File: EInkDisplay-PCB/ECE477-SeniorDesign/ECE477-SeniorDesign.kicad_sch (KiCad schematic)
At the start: 1 part

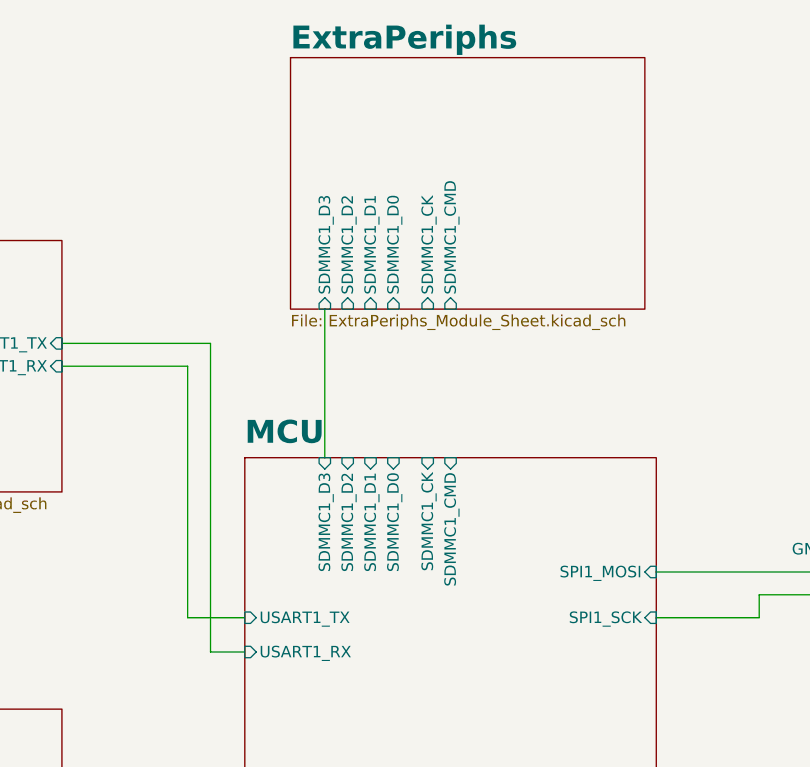
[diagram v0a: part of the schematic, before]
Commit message: Fixing SD w SPI
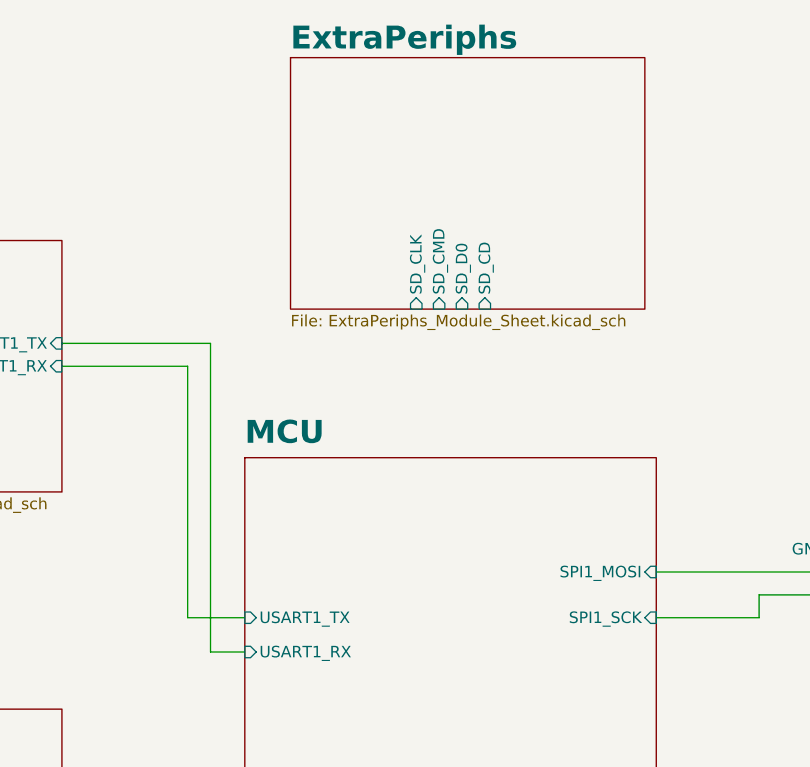
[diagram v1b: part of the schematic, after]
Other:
- sheet ExtraPeriphs ports: added SD_CD, SD_CLK, SD_CMD, SD_D0; removed SDMMC1_CK, SDMMC1_CMD, SDMMC1_D0, SDMMC1_D1, SDMMC1_D2, SDMMC1_D3
- sheet MCU ports: added none; removed SDMMC1_CK, SDMMC1_CMD, SDMMC1_D0, SDMMC1_D1, SDMMC1_D2, SDMMC1_D3
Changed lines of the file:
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@@
-	(wire
-		(pts
-			(xy 125.73 69.85) (xy 125.73 86.36)
-		)
-		(stroke
-			(width 0)
-			(type default)
-		)
-	)
 	(wire
 		(pts
@@
 			)
 		)
-		(pin "SDMMC1_D2" input
-			(at 128.27 69.85 270)
-			(effects
-				(font
-					(size 1.27 1.27)
-				)
-				(justify left)
-			)
-		)
-		(pin "SDMMC1_D3" input
-			(at 125.73 69.85 270)
-			(effects
-				(font
-					(size 1.27 1.27)
-				)
-				(justify left)
-			)
-		)
-		(pin "SDMMC1_D1" input
-			(at 130.81 69.85 270)
-			(effects
-				(font
-					(size 1.27 1.27)
-				)
-				(justify left)
-			)
-		)
-		(pin "SDMMC1_D0" input
-			(at 133.35 69.85 270)
-			(effects
-				(font
-					(size 1.27 1.27)
-				)
-				(justify left)
-			)
-		)
-		(pin "SDMMC1_CK" input
-			(at 137.16 69.85 270)
-			(effects
-				(font
-					(size 1.27 1.27)
-				)
-				(justify left)
-			)
-		)
-		(pin "SDMMC1_CMD" input
-			(at 139.7 69.85 270)
+		(pin "SD_CLK" input
+			(at 135.89 69.85 270)
+			(effects
+				(font
+					(size 1.27 1.27)
+				)
+				(justify left)
+			)
+		)
+		(pin "SD_CMD" input
+			(at 138.43 69.85 270)
+			(effects
+				(font
+					(size 1.27 1.27)
+				)
+				(justify left)
+			)
+		)
+		(pin "SD_D0" input
+			(at 140.97 69.85 270)
+			(effects
+				(font
+					(size 1.27 1.27)
+				)
+				(justify left)
+			)
+		)
+		(pin "SD_CD" input
+			(at 143.51 69.85 270)
 			(effects
 				(font
@@
 			(effects
 				(font
-					(size 1.27 1.27)
-				)
-				(justify right)
-			)
-		)
-		(pin "SDMMC1_CK" input
-			(at 137.16 86.36 90)
-			(effects
-				(font
-					(size 1.27 1.27)
-				)
-				(justify right)
-			)
-		)
-		(pin "SDMMC1_CMD" input
-			(at 139.7 86.36 90)
-			(effects
-				(font
-					(size 1.27 1.27)
-				)
-				(justify right)
-			)
-		)
-		(pin "SDMMC1_D0" input
-			(at 133.35 86.36 90)
-			(effects
-				(font
-					(size 1.27 1.27)
-				)
-				(justify right)
-			)
-		)
-		(pin "SDMMC1_D1" input
-			(at 130.81 86.36 90)
-			(effects
-				(font
-					(size 1.27 1.27)
-				)
-				(justify right)
-			)
-		)
-		(pin "SDMMC1_D2" input
-			(at 128.27 86.36 90)
-			(effects
-				(font
-					(size 1.27 1.27)
-				)
-				(justify right)
-			)
-		)
-		(pin "SDMMC1_D3" input
-			(at 125.73 86.36 90)
-			(effects
-				(font

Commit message: push
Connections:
- net MCU/SPI1_MOSI: no longer EinkDispCon2.3 (DIN)
- net MCU/SPI1_SCK: no longer EinkDispCon2.4 (CLK)
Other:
- sheet ExtraPeriphs ports: added SD_CS, SD_MISO, SD_MOSI, button1, button2, button3; removed SD_CMD, SD_D0
- sheet MCU ports: added SD_GPIO, SPI2_MISO, SPI2_MOSI, SPI2_NSS, SPI2_SCK; removed none
- moved on the sheet: EinkDispCon2
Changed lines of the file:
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@@
+	(wire
+		(pts
+			(xy 133.35 69.85) (xy 133.35 86.36)
+		)
+		(stroke
+			(width 0)
+			(type default)
+		)
+	)
 	(wire
 		(pts
@@
 	(wire
 		(pts
+			(xy 140.97 69.85) (xy 140.97 86.36)
+		)
+		(stroke
+			(width 0)
+			(type default)
+		)
+	)
+	(wire
+		(pts
 			(xy 96.52 76.2) (xy 110.49 76.2)
 		)
@@
 	(wire
 		(pts
-			(xy 173.99 104.14) (xy 173.99 101.6)
-		)
-		(stroke
-			(width 0)
-			(type default)
-		)
-	)
-	(wire
-		(pts
-			(xy 162.56 99.06) (xy 189.23 99.06)
-		)
-		(stroke
-			(width 0)
-			(type default)
-		)
-	)
-	(wire
-		(pts
-			(xy 189.23 93.98) (xy 185.42 93.98)
-		)
-		(stroke
-			(width 0)
-			(type default)
-		)
-	)
-	(wire
-		(pts
-			(xy 185.42 88.9) (xy 185.42 93.98)
+			(xy 130.81 69.85) (xy 130.81 86.36)
+		)
+		(stroke
+			(width 0)
+			(type default)
+		)
+	)
+	(wire
+		(pts
+			(xy 227.33 114.3) (xy 223.52 114.3)
+		)
+		(stroke
+			(width 0)
+			(type default)
+		)
+	)
+	(wire
+		(pts
+			(xy 223.52 109.22) (xy 223.52 114.3)
 		)
 		(stroke
@@
 	(wire
 		(pts
-			(xy 185.42 96.52) (xy 189.23 96.52)
+			(xy 223.52 116.84) (xy 227.33 116.84)
 		)
 		(stroke
@@
 	(wire
 		(pts
-			(xy 173.99 101.6) (xy 189.23 101.6)
-		)
-		(stroke
-			(width 0)
-			(type default)
-		)
-	)
-	(wire
-		(pts
-			(xy 162.56 104.14) (xy 173.99 104.14)
+			(xy 138.43 69.85) (xy 138.43 86.36)
+		)
+		(stroke
+			(width 0)
+			(type default)
+		)
+	)
+	(wire
+		(pts
+			(xy 135.89 69.85) (xy 135.89 86.36)
 		)
 		(stroke
@@
 	(symbol
 		(lib_id "EinkComponentLibrary:EinkDisplay")
-		(at 191.77 128.27 0)
+		(at 229.87 148.59 0)
 		(unit 1)
 		(exclude_from_sim no)
@@
 		(dnp no)
 		(property "Reference" "EinkDispCon2"
-			(at 199.136 116.078 0)
+			(at 237.236 136.398 0)
 			(effects
 				(font
@@
 		)
 		(property "Value" "~"
-			(at 198.12 115.57 0)
+			(at 236.22 135.89 0)
 			(effects
 				(font
@@
 		)
 		(property "Footprint" ""
-			(at 198.12 100.33 0)
+			(at 236.22 120.65 0)
 			(effects
 				(font
@@
 		)
 		(property "Datasheet" ""
-			(at 198.12 100.33 0)
+			(at 236.22 120.65 0)
 			(effects
 				(font
@@
 		)
 		(property "Description" ""
-			(at 198.12 100.33 0)
+			(at 236.22 120.65 0)
 			(effects
 				(font
@@
 	(symbol
 		(lib_id "power:+3.3V")
-		(at 185.42 88.9 0)
+		(at 223.52 109.22 0)
 		(unit 1)
 		(exclude_from_sim no)
@@
 		(fields_autoplaced yes)
 		(property "Reference" "#PWR012"
-			(at 185.42 92.71 0)
+			(at 223.52 113.03 0)
 			(effects
 				(font
@@
 		)
 		(property "Value" "+3.3V"
-			(at 185.42 83.82 0)
+			(at 223.52 104.14 0)
 			(effects
 				(font
@@
 		)
 		(property "Footprint" ""
-			(at 185.42 88.9 0)
+			(at 223.52 109.22 0)
 			(effects
 				(font
@@
 		)
 		(property "Datasheet" ""
-			(at 185.42 88.9 0)
+			(at 223.52 109.22 0)
 			(effects
 				(font
@@
 		)
 		(property "Description" "Power symbol creates a global label with name \"+3.3V\""
-			(at 185.42 88.9 0)
+			(at 223.52 109.22 0)
 			(effects
 				(font
@@
 	(symbol
 		(lib_id "power:GND")
-		(at 185.42 96.52 270)
+		(at 223.52 116.84 270)
 		(unit 1)
 		(exclude_from_sim no)
@@
 		(fields_autoplaced yes)
 		(property "Reference" "#PWR013"
-			(at 179.07 96.52 0)
+			(at 217.17 116.84 0)
 			(effects
 				(font
@@
 		)
 		(property "Value" "GND"
-			(at 181.61 96.5199 90)
+			(at 219.71 116.8399 90)
 			(effects
 				(font
@@
 		)
 		(property "Footprint" ""
-			(at 185.42 96.52 0)
+			(at 223.52 116.84 0)
 			(effects
 				(font
@@
 		)
 		(property "Datasheet" ""
-			(at 185.42 96.52 0)
+			(at 223.52 116.84 0)
 			(effects
 				(font
@@
 		)
 		(property "Description" "Power symbol creates a global label with name \"GND\" , ground"
-			(at 185.42 96.52 0)
+			(at 223.52 116.84 0)
 			(effects
 				(font
@@
 		)
 		(pin "SD_CLK" input
+			(at 130.81 69.85 270)
+			(effects
+				(font
+					(size 1.27 1.27)
+				)
+				(justify left)
+			)
+		)
+		(pin "SD_MOSI" input
+			(at 133.35 69.85 270)
+			(effects
+				(font
+					(size 1.27 1.27)
+				)
+				(justify left)
+			)
+		)
+		(pin "SD_CD" input
+			(at 140.97 69.85 270)
+			(effects
+				(font
+					(size 1.27 1.27)
+				)
+				(justify left)
+			)
+		)
+		(pin "SD_MISO" input
 			(at 135.89 69.85 270)
 			(effects
@@
 			)
 		)
-		(pin "SD_CMD" input
+		(pin "SD_CS" input
 			(at 138.43 69.85 270)
 			(effects
@@
 			)
 		)
-		(pin "SD_D0" input
-			(at 140.97 69.85 270)
-			(effects
-				(font
-					(size 1.27 1.27)
-				)
-				(justify left)
-			)
-		)
-		(pin "SD_CD" input
-			(at 143.51 69.85 270)
+		(pin "button3" input
+			(at 151.13 69.85 270)
+			(effects
+				(font
+					(size 1.27 1.27)
+				)
+				(justify left)
+			)
+		)
+		(pin "button2" input
+			(at 153.67 69.85 270)
+			(effects
+				(font
+					(size 1.27 1.27)
+				)
+				(justify left)
+			)
+		)
+		(pin "button1" input
+			(at 156.21 69.85 270)
 			(effects
 				(font
@@
 	(sheet
 		(at 116.84 86.36)
-		(size 45.72 54.61)
+		(size 66.04 54.61)
 		(fields_autoplaced yes)
 		(stroke
@@
 		)
 		(pin "SPI1_MOSI" input
-			(at 162.56 99.06 0)
+			(at 182.88 121.92 0)
 			(effects
 				(font
@@
 		)
 		(pin "SPI1_SCK" input
-			(at 162.56 104.14 0)
-			(effects
-				(font
+			(at 182.88 127 0)
+			(effects
+				(font
+					(size 1.27 1.27)
+				)
+				(justify right)
+			)
+		)
+		(pin "SPI2_NSS" input
+			(at 138.43 86.36 90)
+			(effects
+				(font
+					(size 1.27 1.27)
+				)
+				(justify right)
+			)
+		)
+		(pin "SPI2_SCK" input
+			(at 130.81 86.36 90)
+			(effects
+				(font
+					(size 1.27 1.27)
+				)
+				(justify right)
+			)
+		)
+		(pin "SPI2_MISO" input
+			(at 135.89 86.36 90)
+			(effects
+				(font
+					(size 1.27 1.27)
+				)
+				(justify right)
+			)
+		)
+		(pin "SPI2_MOSI" input
+			(at 133.35 86.36 90)
+			(effects
+				(font
+					(size 1.27 1.27)
+				)
+				(justify right)
+			)
+		)
+		(pin "SD_GPIO" input
+			(at 140.97 86.36 90)
+			(effects
+				(font

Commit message: Changes
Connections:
- net MCU/SPI1_MOSI: now also EinkDispCon2.3 (DIN)
- net MCU/SPI1_SCK: now also EinkDispCon2.4 (CLK)
- net MCU/SPI1_NSS: now reaches EinkDispCon2.5 (CS)
- net MCU/Eink_D/C: now reaches EinkDispCon2.6 (D/C)
- net MCU/Eink_RST: now reaches EinkDispCon2.7 (RST)
- net MCU/Eink_Busy: now reaches EinkDispCon2.8 (BUSY)
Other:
- sheet MCU ports: added Eink_Busy, Eink_D/C, Eink_RST, SPI1_NSS, button1, button2, button3; removed none
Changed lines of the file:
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@@
+	(wire
+		(pts
+			(xy 182.88 124.46) (xy 227.33 124.46)
+		)
+		(stroke
+			(width 0)
+			(type default)
+		)
+	)
 	(wire
 		(pts
@@
 	(wire
 		(pts
+			(xy 151.13 69.85) (xy 151.13 86.36)
+		)
+		(stroke
+			(width 0)
+			(type default)
+		)
+	)
+	(wire
+		(pts
 			(xy 227.33 114.3) (xy 223.52 114.3)
 		)
@@
 	(wire
 		(pts
+			(xy 182.88 119.38) (xy 227.33 119.38)
+		)
+		(stroke
+			(width 0)
+			(type default)
+		)
+	)
+	(wire
+		(pts
 			(xy 96.52 73.66) (xy 113.03 73.66)
 		)
@@
 	(wire
 		(pts
+			(xy 156.21 69.85) (xy 156.21 86.36)
+		)
+		(stroke
+			(width 0)
+			(type default)
+		)
+	)
+	(wire
+		(pts
+			(xy 153.67 69.85) (xy 153.67 86.36)
+		)
+		(stroke
+			(width 0)
+			(type default)
+		)
+	)
+	(wire
+		(pts
+			(xy 182.88 132.08) (xy 227.33 132.08)
+		)
+		(stroke
+			(width 0)
+			(type default)
+		)
+	)
+	(wire
+		(pts
+			(xy 182.88 127) (xy 227.33 127)
+		)
+		(stroke
+			(width 0)
+			(type default)
+		)
+	)
+	(wire
+		(pts
 			(xy 138.43 69.85) (xy 138.43 86.36)
+		)
+		(stroke
+			(width 0)
+			(type default)
+		)
+	)
+	(wire
+		(pts
+			(xy 182.88 121.92) (xy 227.33 121.92)
+		)
+		(stroke
+			(width 0)
+			(type default)
+		)
+	)
+	(wire
+		(pts
+			(xy 182.88 129.54) (xy 227.33 129.54)
 		)
 		(stroke
@@
 			)
 		)
-		(pin "SPI1_MOSI" input
-			(at 182.88 121.92 0)
-			(effects
-				(font
-					(size 1.27 1.27)
-				)
-				(justify right)
-			)
-		)
-		(pin "SPI1_SCK" input
-			(at 182.88 127 0)
-			(effects
-				(font
-					(size 1.27 1.27)
-				)
-				(justify right)
-			)
-		)
 		(pin "SPI2_NSS" input
 			(at 138.43 86.36 90)
@@
 			(effects
 				(font
+					(size 1.27 1.27)
+				)
+				(justify right)
+			)
+		)
+		(pin "SPI1_NSS" input
+			(at 182.88 124.46 0)
+			(effects
+				(font
+					(size 1.27 1.27)
+				)
+				(justify right)
+			)
+		)
+		(pin "SPI1_SCK" input
+			(at 182.88 121.92 0)
+			(effects
+				(font
+					(size 1.27 1.27)
+				)
+				(justify right)
+			)
+		)
+		(pin "SPI1_MOSI" input
+			(at 182.88 119.38 0)
+			(effects
+				(font
+					(size 1.27 1.27)
+				)
+				(justify right)
+			)
+		)
+		(pin "Eink_Busy" input
+			(at 182.88 132.08 0)
+			(effects
+				(font
+					(size 1.27 1.27)
+				)
+				(justify right)
+			)
+		)
+		(pin "Eink_D{slash}C" input
+			(at 182.88 127 0)
+			(effects
+				(font
+					(size 1.27 1.27)
+				)
+				(justify right)
+			)
+		)
+		(pin "Eink_RST" input
+			(at 182.88 129.54 0)
+			(effects
+				(font
+					(size 1.27 1.27)
+				)
+				(justify right)
+			)
+		)
+		(pin "button1" input
+			(at 156.21 86.36 90)
+			(effects
+				(font
+					(size 1.27 1.27)
+				)
+				(justify right)
+			)
+		)
+		(pin "button2" input
+			(at 153.67 86.36 90)
+			(effects
+				(font
+					(size 1.27 1.27)
+				)
+				(justify right)
+			)
+		)
+		(pin "button3" input
+			(at 151.13 86.36 90)
+			(effects
+				(font

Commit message: push
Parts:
- added TP10: E_RST, symbol Connector:TestPoint
- added TP11: E_Busy, symbol Connector:TestPoint
- added TP12: UART_TX, symbol Connector:TestPoint
- added TP13: UART_RX, symbol Connector:TestPoint
- added TP6: E_MOSI, symbol Connector:TestPoint
- added TP7: E_SCK, symbol Connector:TestPoint
- added TP8: E_NSS, symbol Connector:TestPoint
- added TP9: E_D/C, symbol Connector:TestPoint
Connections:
- net MCU/Eink_Busy: now also TP11.1
- net MCU/Eink_D/C: now also TP9.1
- net MCU/Eink_RST: now also TP10.1
- net MCU/SPI1_MOSI: now also TP6.1
- net MCU/SPI1_NSS: now also TP8.1
- net MCU/SPI1_SCK: now also TP7.1
- net MCU/USART1_RX: now also TP12.1
- net MCU/USART1_TX: now also TP13.1

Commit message: fixing things
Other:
- sheet LipoPower ports: added Monitor_GPOUT, Monitor_SCL, Monitor_SDA, Recharge_PG, Recharge_ST1, Recharge_ST2; removed none
- sheet MCU ports: added GPIO_1, GPIO_2, GPIO_3, GPIO_4, GPIO_5, GPIO_6; removed none
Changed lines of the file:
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@@
+	(wire
+		(pts
+			(xy 96.52 123.19) (xy 116.84 123.19)
+		)
+		(stroke
+			(width 0)
+			(type default)
+		)
+	)
 	(wire
 		(pts
@@
 	(wire
 		(pts
+			(xy 96.52 132.08) (xy 116.84 132.08)
+		)
+		(stroke
+			(width 0)
+			(type default)
+		)
+	)
+	(wire
+		(pts
+			(xy 96.52 134.62) (xy 116.84 134.62)
+		)
+		(stroke
+			(width 0)
+			(type default)
+		)
+	)
+	(wire
+		(pts
 			(xy 151.13 69.85) (xy 151.13 86.36)
 		)
@@
 	(wire
 		(pts
+			(xy 96.52 120.65) (xy 116.84 120.65)
+		)
+		(stroke
+			(width 0)
+			(type default)
+		)
+	)
+	(wire
+		(pts
 			(xy 227.33 114.3) (xy 223.52 114.3)
 		)
@@
 	(wire
 		(pts
+			(xy 96.52 129.54) (xy 116.84 129.54)
+		)
+		(stroke
+			(width 0)
+			(type default)
+		)
+	)
+	(wire
+		(pts
 			(xy 113.03 107.95) (xy 116.84 107.95)
 		)
@@
 		(pts
 			(xy 99.06 73.66) (xy 113.03 73.66)
+		)
+		(stroke
+			(width 0)
+			(type default)
+		)
+	)
+	(wire
+		(pts
+			(xy 96.52 118.11) (xy 116.84 118.11)
 		)
 		(stroke
@@
 			)
 		)
+		(pin "GPIO_1" input
+			(at 116.84 118.11 180)
+			(effects
+				(font
+					(size 1.27 1.27)
+				)
+				(justify left)
+			)
+		)
+		(pin "GPIO_5" input
+			(at 116.84 120.65 180)
+			(effects
+				(font
+					(size 1.27 1.27)
+				)
+				(justify left)
+			)
+		)
+		(pin "GPIO_2" input
+			(at 116.84 123.19 180)
+			(effects
+				(font
+					(size 1.27 1.27)
+				)
+				(justify left)
+			)
+		)
+		(pin "GPIO_3" input
+			(at 116.84 129.54 180)
+			(effects
+				(font
+					(size 1.27 1.27)
+				)
+				(justify left)
+			)
+		)
+		(pin "GPIO_4" input
+			(at 116.84 132.08 180)
+			(effects
+				(font
+					(size 1.27 1.27)
+				)
+				(justify left)
+			)
+		)
+		(pin "GPIO_6" input
+			(at 116.84 134.62 180)
+			(effects
+				(font
+					(size 1.27 1.27)
+				)
+				(justify left)
+			)
+		)
 		(instances
 			(project "ECE477-SeniorDesign"
@@
 			)
 		)
+		(pin "Monitor_SCL" input
+			(at 96.52 118.11 0)
+			(effects
+				(font
+					(size 1.27 1.27)
+				)
+				(justify right)
+			)
+		)
+		(pin "Monitor_SDA" input
+			(at 96.52 120.65 0)
+			(effects
+				(font
+					(size 1.27 1.27)
+				)
+				(justify right)
+			)
+		)
+		(pin "Monitor_GPOUT" input
+			(at 96.52 123.19 0)
+			(effects
+				(font
+					(size 1.27 1.27)
+				)
+				(justify right)
+			)
+		)
+		(pin "Recharge_PG" input
+			(at 96.52 129.54 0)
+			(effects
+				(font
+					(size 1.27 1.27)
+				)
+				(justify right)
+			)
+		)
+		(pin "Recharge_ST1" input
+			(at 96.52 132.08 0)
+			(effects
+				(font
+					(size 1.27 1.27)
+				)
+				(justify right)
+			)
+		)
+		(pin "Recharge_ST2" input
+			(at 96.52 134.62 0)
+			(effects
+				(font
+					(size 1.27 1.27)
+				)
+				(justify right)
+			)
+		)

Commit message: Lotta changes
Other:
- sheet MCU ports: added I2C2_SCL, I2C2_SDA; removed GPIO_1, GPIO_2

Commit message: SD card updates
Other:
- sheet ExtraPeriphs ports: added SD_SCK; removed SD_CD, SD_CLK
- sheet MCU ports: added none; removed SD_GPIO
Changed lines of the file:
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@@
-	(wire
-		(pts
-			(xy 140.97 69.85) (xy 140.97 86.36)
-		)
-		(stroke
-			(width 0)
-			(type default)
-		)
-	)
 	(wire
 		(pts
@@
 			)
 		)
-		(pin "SD_CLK" input
+		(pin "button3" input
+			(at 151.13 69.85 270)
+			(effects
+				(font
+					(size 1.27 1.27)
+				)
+				(justify left)
+			)
+		)
+		(pin "button2" input
+			(at 153.67 69.85 270)
+			(effects
+				(font
+					(size 1.27 1.27)
+				)
+				(justify left)
+			)
+		)
+		(pin "button1" input
+			(at 156.21 69.85 270)
+			(effects
+				(font
+					(size 1.27 1.27)
+				)
+				(justify left)
+			)
+		)
+		(pin "SD_SCK" input
 			(at 130.81 69.85 270)
 			(effects
@@
 			)
 		)
-		(pin "SD_CD" input
-			(at 140.97 69.85 270)
-			(effects
-				(font
-					(size 1.27 1.27)
-				)
-				(justify left)
-			)
-		)
 		(pin "SD_MISO" input
 			(at 135.89 69.85 270)
@@
 		(pin "SD_CS" input
 			(at 138.43 69.85 270)
-			(effects
-				(font
-					(size 1.27 1.27)
-				)
-				(justify left)
-			)
-		)
-		(pin "button3" input
-			(at 151.13 69.85 270)
-			(effects
-				(font
-					(size 1.27 1.27)
-				)
-				(justify left)
-			)
-		)
-		(pin "button2" input
-			(at 153.67 69.85 270)
-			(effects
-				(font
-					(size 1.27 1.27)
-				)
-				(justify left)
-			)
-		)
-		(pin "button1" input
-			(at 156.21 69.85 270)
 			(effects
 				(font
@@
 			(effects
 				(font
-					(size 1.27 1.27)
-				)
-				(justify right)
-			)
-		)
-		(pin "SD_GPIO" input
-			(at 140.97 86.36 90)
-			(effects
-				(font

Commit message: changes
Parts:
- added H1, H2, H3, H4: MountingHole, symbol Mechanical:MountingHole
